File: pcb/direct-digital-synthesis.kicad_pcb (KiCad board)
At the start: 4 copper layers, 155.9 x 106.6 mm, 204 parts, among them IC1 IS42S16160J-7TLI, J1 TagConnect_TC2030, J2 Barrel_Jack_Switch, J3 MEM2061-01-188-00-A, J4 BNC_Connector, J5 Conn_01x07_Socket, Q1 PMPB27EPZ, SW1 SW_Push, SW2 SW_Push, U1 STM32H750IBT6, U10 PEC12R-3225F-S0024, U11 MCP45HV51-ST, U12 TLV07IDR, U2 PCHCS541QWRKSRQ1, U3 PCHCS541QWRKSRQ1, U4 AD5445YCPZ, U5 LTC3260EDE-PBF, U6 REF5010AID, U7 LMR36015FBRNXR, U8 AD8066ARZ-R7, U9 AD8066ARZ-R7, Y1 ECS-2520MVQ-240-BS-TR

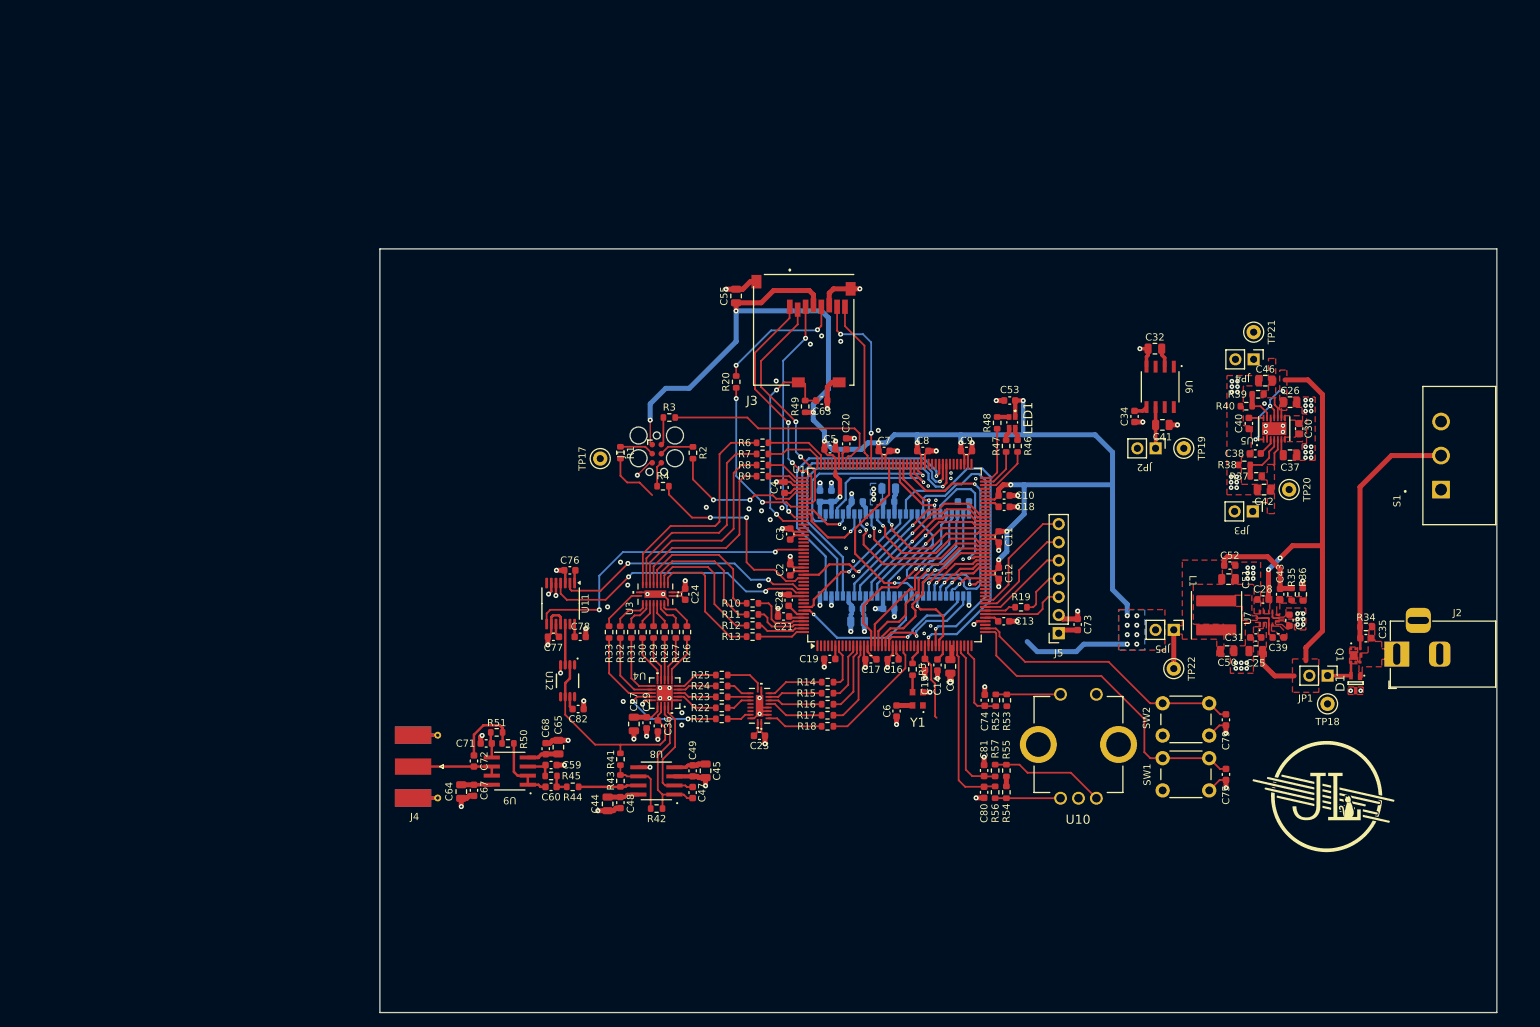
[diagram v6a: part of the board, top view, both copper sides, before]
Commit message: fixed sdram
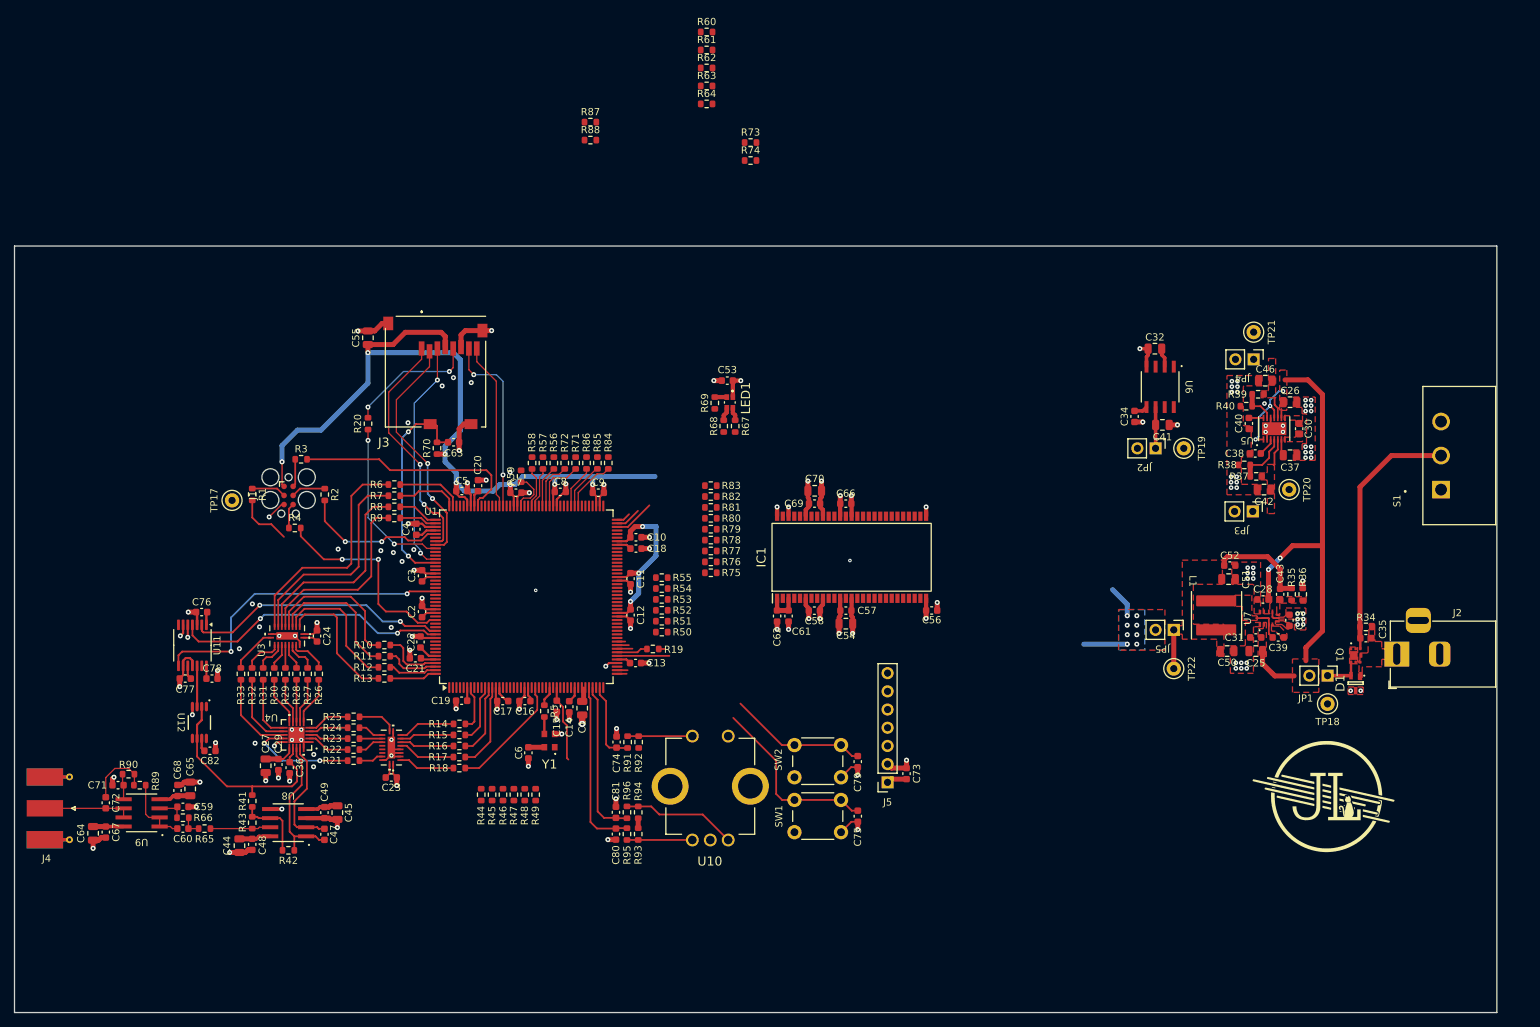
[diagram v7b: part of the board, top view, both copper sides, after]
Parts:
- added R44: 22R, Resistor_SMD:R_0603_1608Metric, F.Cu at (250.0, 221.4)
- added R45: 22R, Resistor_SMD:R_0603_1608Metric, F.Cu at (251.6, 221.4)
- added R46: 22R, Resistor_SMD:R_0603_1608Metric, F.Cu at (253.1, 221.4)
- added R47: 22R, Resistor_SMD:R_0603_1608Metric, F.Cu at (254.6, 221.4)
- added R48: 22R, Resistor_SMD:R_0603_1608Metric, F.Cu at (256.1, 221.4)
- added R49: 22R, Resistor_SMD:R_0603_1608Metric, F.Cu at (257.6, 221.4)
- added R50: 22R, Resistor_SMD:R_0603_1608Metric, F.Cu at (275.2, 198.7)
- added R51: 22R, Resistor_SMD:R_0603_1608Metric, F.Cu at (275.2, 197.2)
- added R52: 22R, Resistor_SMD:R_0603_1608Metric, F.Cu at (275.2, 195.6)
- added R53: 22R, Resistor_SMD:R_0603_1608Metric, F.Cu at (275.2, 194.1)
- added R54: 22R, Resistor_SMD:R_0603_1608Metric, F.Cu at (275.2, 192.6)
- added R55: 22R, Resistor_SMD:R_0603_1608Metric, F.Cu at (275.2, 191.1)
- added R56: 22R, Resistor_SMD:R_0603_1608Metric, F.Cu at (260.2, 175.1)
- added R57: 22R, Resistor_SMD:R_0603_1608Metric, F.Cu at (258.6, 175.1)
- added R58: 22R, Resistor_SMD:R_0603_1608Metric, F.Cu at (257.1, 175.1)
- added R59: 22R, Resistor_SMD:R_0603_1608Metric, F.Cu at (255.6, 176.9)
- added R60: 22R, Resistor_SMD:R_0603_1608Metric, F.Cu at (281.5, 114.9)
- added R61: 22R, Resistor_SMD:R_0603_1608Metric, F.Cu at (281.5, 117.4)
- added R62: 22R, Resistor_SMD:R_0603_1608Metric, F.Cu at (281.5, 119.9)
- added R63: 22R, Resistor_SMD:R_0603_1608Metric, F.Cu at (281.5, 122.5)
- added R64: 22R, Resistor_SMD:R_0603_1608Metric, F.Cu at (281.5, 125.0)
- added R71: 22R, Resistor_SMD:R_0603_1608Metric, F.Cu at (263.2, 175.1)
- added R72: 22R, Resistor_SMD:R_0603_1608Metric, F.Cu at (261.7, 175.1)
- added R73: 22R, Resistor_SMD:R_0603_1608Metric, F.Cu at (287.6, 130.3)
- added R74: 22R, Resistor_SMD:R_0603_1608Metric, F.Cu at (287.6, 132.9)
- added R75: 22R, Resistor_SMD:R_0603_1608Metric, F.Cu at (282.1, 190.4)
- added R76: 22R, Resistor_SMD:R_0603_1608Metric, F.Cu at (282.1, 188.9)
- added R77: 22R, Resistor_SMD:R_0603_1608Metric, F.Cu at (282.1, 187.4)
- added R78: 22R, Resistor_SMD:R_0603_1608Metric, F.Cu at (282.1, 185.8)
- added R79: 22R, Resistor_SMD:R_0603_1608Metric, F.Cu at (282.1, 184.3)
- added R80: 22R, Resistor_SMD:R_0603_1608Metric, F.Cu at (282.1, 182.8)
- added R81: 22R, Resistor_SMD:R_0603_1608Metric, F.Cu at (282.1, 181.3)
- added R82: 22R, Resistor_SMD:R_0603_1608Metric, F.Cu at (282.1, 179.8)
- added R83: 22R, Resistor_SMD:R_0603_1608Metric, F.Cu at (282.1, 178.2)
- added R84: 22R, Resistor_SMD:R_0603_1608Metric, F.Cu at (267.8, 175.1)
- added R85: 22R, Resistor_SMD:R_0603_1608Metric, F.Cu at (266.2, 175.1)
- added R86: 22R, Resistor_SMD:R_0603_1608Metric, F.Cu at (264.7, 175.1)
- added R87: 22R, Resistor_SMD:R_0603_1608Metric, F.Cu at (265.3, 127.5)
- added R88: 22R, Resistor_SMD:R_0603_1608Metric, F.Cu at (265.3, 130.0)
- C54, C56, C57, C58, C61, C62, C66, C69, C70, IC1: moved to F.Cu
- moved C79 51.7 mm to (302.6, 216.8)
- moved C80 51.7 mm to (268.8, 226.9)
- moved C81 51.7 mm to (268.8, 223.8)
- moved R91 51.7 mm to (270.5, 214.0)
- moved C17 51.7 mm to (253.0, 208.3)
- moved C19 51.7 mm to (247.3, 208.3)
- moved C2 51.7 mm to (241.8, 195.8)
- moved C20 51.7 mm to (249.6, 178.2)
- moved C21 51.7 mm to (240.8, 202.3)
- moved C23 51.7 mm to (237.5, 219.0)
- moved C29 51.7 mm to (221.7, 217.2)
- moved C3 51.7 mm to (241.8, 190.8)
- moved C4 51.7 mm to (241.0, 184.3)
- moved C44 51.7 mm to (216.3, 228.5)
- moved C47 51.7 mm to (228.2, 226.9)
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- renumbered R44 to R65, R45 to R66, R46 to R67, R47 to R68, R48 to R69, R49 to R70, R50 to R89, R51 to R90, R52 to R91, R53 to R92, R54 to R93, R55 to R94, R56 to R95, R57 to R96
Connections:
- IC1 pad 10: /SDRAM.DQ5 -> Net-(IC1-DQ5)
- IC1 pad 11: /SDRAM.DQ6 -> Net-(IC1-DQ6)
- IC1 pad 13: /SDRAM.DQ7 -> Net-(IC1-DQ7)
- IC1 pad 15: /SDRAM_DQML -> Net-(IC1-DQML)
- IC1 pad 16: /SDRAM_NWE -> Net-(IC1-~{WE})
- IC1 pad 17: /SDRAM_NCAS -> Net-(IC1-~{CAS})
- IC1 pad 18: /SDRAM_NRAS -> Net-(IC1-~{RAS})
- IC1 pad 19: /SDRAM_NCS -> Net-(IC1-~{CS})
- IC1 pad 2: /SDRAM.DQ0 -> Net-(IC1-DQ0)
- IC1 pad 20: /SDRAM_BA0 -> Net-(IC1-BA0)
- IC1 pad 21: /SDRAM_BA1 -> Net-(IC1-BA1)
- IC1 pad 22: /SDRAM_A10 -> Net-(IC1-A10)
- IC1 pad 23: /SDRAM_A0 -> Net-(IC1-A0)
- IC1 pad 24: /SDRAM_A1 -> Net-(IC1-A1)
- IC1 pad 25: /SDRAM_A2 -> Net-(IC1-A2)
- IC1 pad 26: /SDRAM_A3 -> Net-(IC1-A3)
- IC1 pad 29: /SDRAM_A4 -> Net-(IC1-A4)
- IC1 pad 30: /SDRAM_A5 -> Net-(IC1-A5)
- IC1 pad 31: /SDRAM_A6 -> Net-(IC1-A6)
- IC1 pad 32: /SDRAM_A7 -> Net-(IC1-A7)
- IC1 pad 33: /SDRAM_A8 -> Net-(IC1-A8)
- IC1 pad 34: /SDRAM_A9 -> Net-(IC1-A9)
- IC1 pad 35: /SDRAM_A11 -> Net-(IC1-A11)
- IC1 pad 36: /SDRAM_A12 -> Net-(IC1-A12)
- IC1 pad 37: /SDRAM_CKE -> Net-(IC1-CKE)
- IC1 pad 38: /SDRAM_CLK -> Net-(IC1-CLK)
- IC1 pad 39: /SDRAM_DQMH -> Net-(IC1-DQMH)
- IC1 pad 4: /SDRAM.DQ1 -> Net-(IC1-DQ1)
- IC1 pad 42: /SDRAM.DQ8 -> Net-(IC1-DQ8)
- IC1 pad 44: /SDRAM.DQ9 -> Net-(IC1-DQ9)
- IC1 pad 45: /SDRAM.DQ10 -> Net-(IC1-DQ10)
- IC1 pad 47: /SDRAM.DQ11 -> Net-(IC1-DQ11)
- IC1 pad 48: /SDRAM.DQ12 -> Net-(IC1-DQ12)
- IC1 pad 5: /SDRAM.DQ2 -> Net-(IC1-DQ2)
- IC1 pad 50: /SDRAM.DQ13 -> Net-(IC1-DQ13)
- IC1 pad 51: /SDRAM.DQ14 -> Net-(IC1-DQ14)
- IC1 pad 53: /SDRAM.DQ15 -> Net-(IC1-DQ15)
- IC1 pad 7: /SDRAM.DQ3 -> Net-(IC1-DQ3)
- IC1 pad 8: /SDRAM.DQ4 -> Net-(IC1-DQ4)
- U1 pad 106: /SDRAM_A12 -> /SDRAM.A12
- U1 pad 108: /SDRAM_BA0 -> /SDRAM.BA0
- U1 pad 109: /SDRAM_BA1 -> /SDRAM.BA1
- U1 pad 112: /SDRAM_CLK -> /SDRAM.CLK
- U1 pad 16: /SDRAM_A0 -> /SDRAM.A0
- U1 pad 160: /SDRAM_NCAS -> /SDRAM.NCAS
- U1 pad 169: /SDRAM_DQML -> /SDRAM.DQML
- U1 pad 17: /SDRAM_A1 -> /SDRAM.A1
- U1 pad 170: /SDRAM_DQMH -> /SDRAM.DQMH
- U1 pad 18: /SDRAM_A2 -> /SDRAM.A2
- U1 pad 19: /SDRAM_A3 -> /SDRAM.A3
- U1 pad 20: /SDRAM_A4 -> /SDRAM.A4
- U1 pad 21: /SDRAM_A5 -> /SDRAM.A5
- U1 pad 32: /SDRAM_NWE -> /SDRAM.NWE
- U1 pad 34: /SDRAM_NCS -> /SDRAM.NCS
- U1 pad 35: /SDRAM_CKE -> /SDRAM.CKE
- U1 pad 59: /SDRAM_NRAS -> /SDRAM.NRAS
- U1 pad 60: /SDRAM_A6 -> /SDRAM.A6
- U1 pad 63: /SDRAM_A7 -> /SDRAM.A7
- U1 pad 64: /SDRAM_A8 -> /SDRAM.A8
- U1 pad 65: /SDRAM_A9 -> /SDRAM.A9
- U1 pad 66: /SDRAM_A10 -> /SDRAM.A10
- U1 pad 67: /SDRAM_A11 -> /SDRAM.A11
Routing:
- net +3.3V: track 283.3 -> 221.3 mm, vias 22 -> 24
- net /SDRAM_NWE: track 45.2 -> 0.00 mm, vias 1 -> 0
- net /SDRAM_NCS: track 40.0 -> 0.00 mm, vias 1 -> 0
- net /SDRAM_A12: track 37.5 -> 0.00 mm, vias 1 -> 0
- net /SDRAM.DQ15: track 42.6 -> 6.07 mm, vias 1 -> 0
- net /SDRAM.DQ14: track 43.1 -> 6.58 mm, vias 1 -> 0
- net /SDRAM.DQ13: track 42.9 -> 7.43 mm, vias 1 -> 0
- net /SDRAM_CLK: track 25.5 -> 0.00 mm, vias 1 -> 0
- net /SDRAM.DQ12: track 25.2 -> 0.00 mm, vias 1 -> 0
- net /SDRAM_A3: track 24.9 -> 0.00 mm, vias 1 -> 0
- net /SDRAM_A0: track 24.9 -> 0.00 mm, vias 1 -> 0
- net /SDRAM_A2: track 24.5 -> 0.00 mm, vias 1 -> 0
- net /SDRAM.DQ4: track 23.9 -> 0.00 mm, vias 1 -> 0
- net /SDRAM.DQ11: track 23.8 -> 0.00 mm, vias 1 -> 0
- net /SDRAM_A1: track 23.5 -> 0.00 mm, vias 1 -> 0
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- removed copper zone on B.Cu, net GND
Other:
- board size 155.9 x 106.6 mm -> 206.9 x 107 mm
